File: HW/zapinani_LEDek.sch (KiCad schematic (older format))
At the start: 12 parts, among them Q4 Q_NMOS_GSD, Q5 Q_PMOS_GSD, Q6 Q_NMOS_GSD, Q7 Q_PMOS_GSD, Q8 Q_NMOS_GSD, Q9 Q_PMOS_GSD

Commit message: move mounting holes, move power LED 3V3
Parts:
- Q5, Q7, Q9: LCSC C15127 -> C10487
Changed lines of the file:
@@
 F 2 "Package_TO_SOT_SMD:SOT-23" H 2850 3400 50  0001 C CNN
 F 3 "~" H 2650 3300 50  0001 C CNN
-F 4 "C15127" H 2650 3300 50  0001 C CNN "LCSC"
+F 4 "C10487" H 2650 3300 50  0001 C CNN "LCSC"
 F 5 "0;0;180" H 2650 3300 50  0001 C CNN "JLCPCB_CORRECTION"
 	1    2650 3300
@@
 F 2 "Package_TO_SOT_SMD:SOT-23" H 5900 3400 50  0001 C CNN
 F 3 "~" H 5700 3300 50  0001 C CNN
-F 4 "C15127" H 5700 3300 50  0001 C CNN "LCSC"
+F 4 "C10487" H 5700 3300 50  0001 C CNN "LCSC"
 F 5 "0;0;180" H 5700 3300 50  0001 C CNN "JLCPCB_CORRECTION"
 	1    5700 3300
@@
 F 2 "Package_TO_SOT_SMD:SOT-23" H 8750 3400 50  0001 C CNN
 F 3 "~" H 8550 3300 50  0001 C CNN
-F 4 "C15127" H 8550 3300 50  0001 C CNN "LCSC"
+F 4 "C10487" H 8550 3300 50  0001 C CNN "LCSC"
 F 5 "0;0;180" H 8550 3300 50  0001 C CNN "JLCPCB_CORRECTION"
 	1    8550 3300

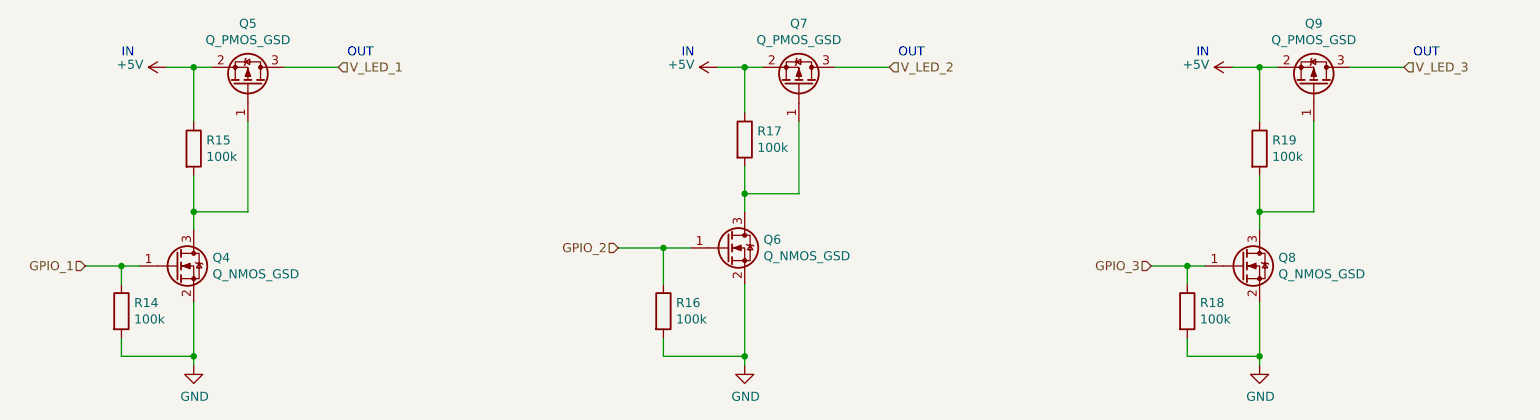
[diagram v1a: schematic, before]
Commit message: make schematic beautiful (for printing)
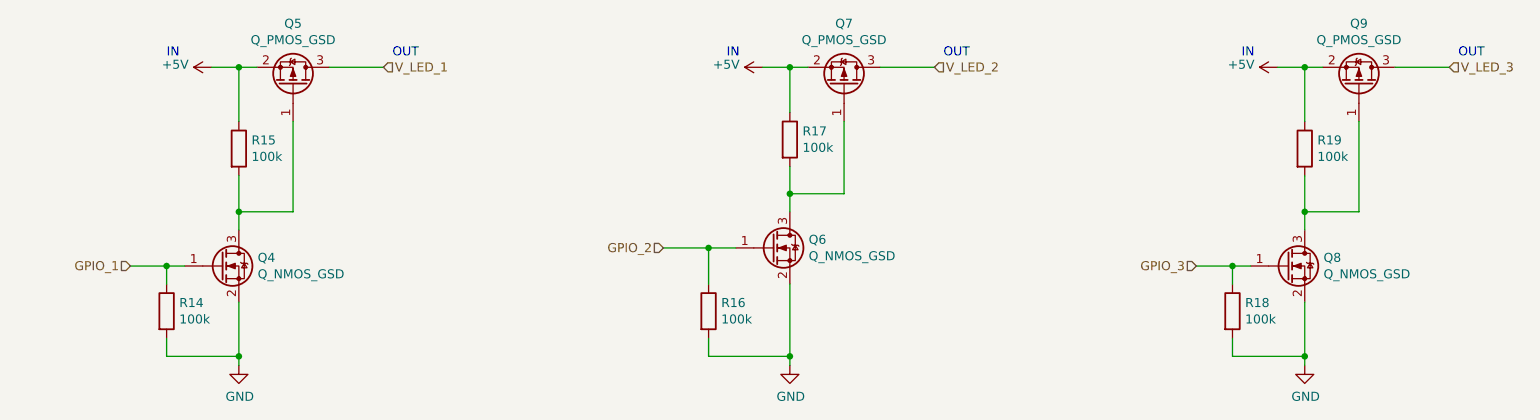
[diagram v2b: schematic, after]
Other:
- moved on the sheet: Q4, Q5, Q6, Q7, Q8, Q9, R14, R15, R16, R17, R18, R19
